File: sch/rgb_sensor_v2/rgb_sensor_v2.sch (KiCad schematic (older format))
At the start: 57 parts, among them J1 Conn_01x20_Male, Q1 2N7002, Q2 2N7002, Q3 2N7002, Q4 2N7002, Q5 2N7002, U1 TCS34725FN, U2 TCS34725FN, U3 TCS34725FN, U4 TCS34725FN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

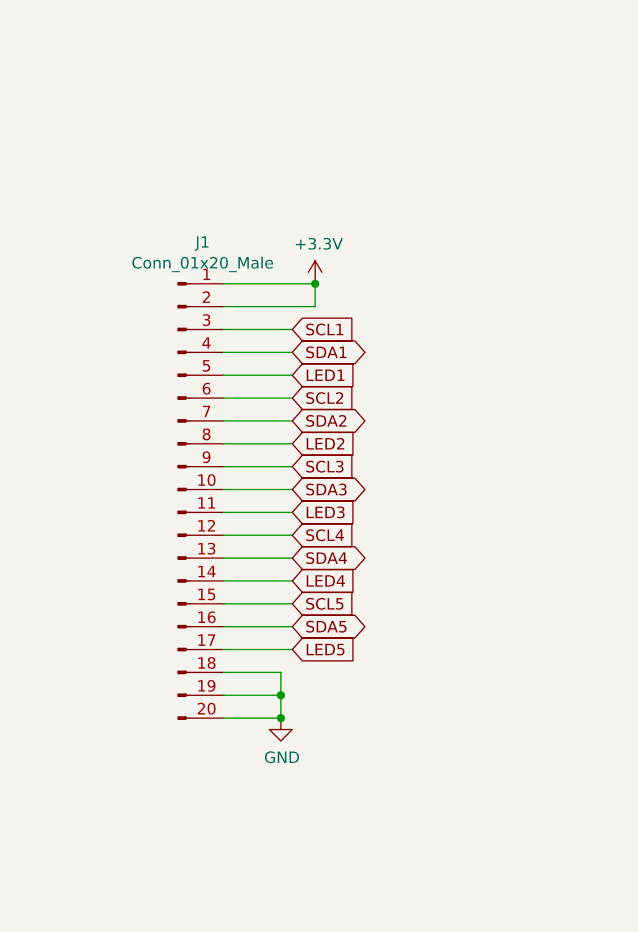
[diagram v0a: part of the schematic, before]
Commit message: some layout done
beefore changing pin assignment on main connector
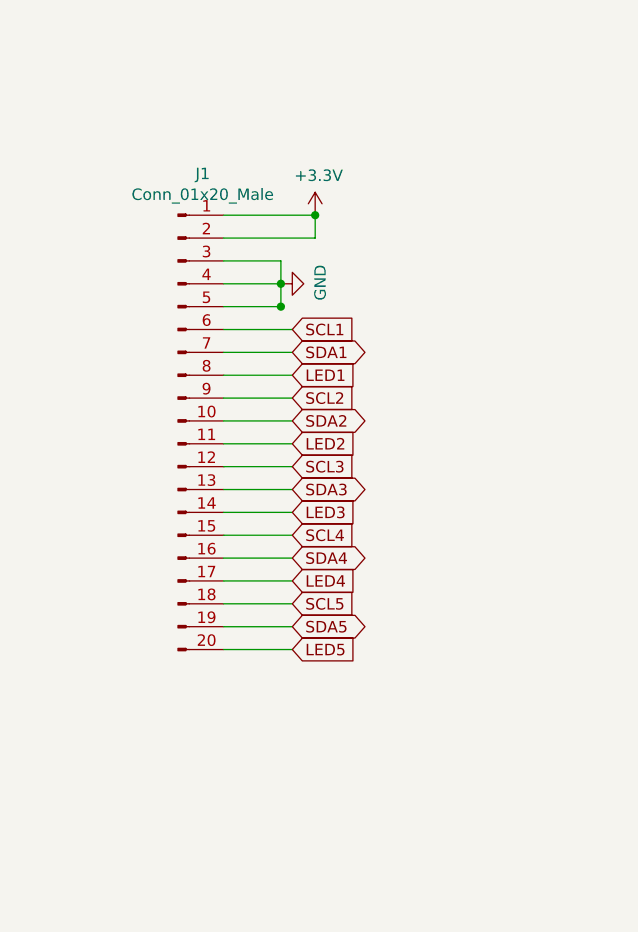
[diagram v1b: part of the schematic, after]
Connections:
- net GND: now also J1.3 (Pin_3), J1.4 (Pin_4), J1.5 (Pin_5); no longer J1.18 (Pin_18), J1.19 (Pin_19), J1.20 (Pin_20)
- net LED1: now also J1.8 (Pin_8); no longer J1.5 (Pin_5)
- net LED2: now also J1.11 (Pin_11); no longer J1.8 (Pin_8)
- net LED3: now also J1.14 (Pin_14); no longer J1.11 (Pin_11)
- net LED4: now also J1.17 (Pin_17); no longer J1.14 (Pin_14)
- net LED5: now also J1.20 (Pin_20); no longer J1.17 (Pin_17)
- net SCL1: now also J1.6 (Pin_6); no longer J1.3 (Pin_3)
- net SCL2: now also J1.9 (Pin_9); no longer J1.6 (Pin_6)
- net SCL3: now also J1.12 (Pin_12); no longer J1.9 (Pin_9)
- net SCL4: now also J1.15 (Pin_15); no longer J1.12 (Pin_12)
- net SCL5: now also J1.18 (Pin_18); no longer J1.15 (Pin_15)
- net SDA1: now also J1.7 (Pin_7); no longer J1.4 (Pin_4)
- net SDA2: now also J1.10 (Pin_10); no longer J1.7 (Pin_7)
- net SDA3: now also J1.13 (Pin_13); no longer J1.10 (Pin_10)
- net SDA4: now also J1.16 (Pin_16); no longer J1.13 (Pin_13)
- net SDA5: now also J1.19 (Pin_19); no longer J1.16 (Pin_16)
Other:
- moved on the sheet: J1
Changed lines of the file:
@@
 L power:+3.3V #PWR021
 U 1 1 5FB4782C
-P 2350 4350
-F 0 "#PWR021" H 2350 4200 50  0001 C CNN
-F 1 "+3.3V" H 2365 4523 50  0000 C CNN
-F 2 "" H 2350 4350 50  0001 C CNN
-F 3 "" H 2350 4350 50  0001 C CNN
-	1    2350 4350
+P 2350 4050
+F 0 "#PWR021" H 2350 3900 50  0001 C CNN
+F 1 "+3.3V" H 2365 4223 50  0000 C CNN
+F 2 "" H 2350 4050 50  0001 C CNN
+F 3 "" H 2350 4050 50  0001 C CNN
+	1    2350 4050
 	1    0    0    -1
 $EndComp
@@
 L power:GND #PWR032
 U 1 1 5FB48129
-P 2200 6250
-F 0 "#PWR032" H 2200 6000 50  0001 C CNN
-F 1 "GND" H 2205 6077 50  0000 C CNN
-F 2 "" H 2200 6250 50  0001 C CNN
-F 3 "" H 2200 6250 50  0001 C CNN
-	1    2200 6250
-	1    0    0    -1
+P 2200 4350
+F 0 "#PWR032" H 2200 4100 50  0001 C CNN
+F 1 "GND" H 2205 4177 50  0000 C CNN
+F 2 "" H 2200 4350 50  0001 C CNN
+F 3 "" H 2200 4350 50  0001 C CNN
+	1    2200 4350
+	0    -1   -1   0
 $EndComp
 Wire Wire Line
@@
 L Connector:Conn_01x20_Male J1
 U 1 1 5FB2920F
-P 1750 5250
-F 0 "J1" H 1858 6331 50  0000 C CNN
-F 1 "Conn_01x20_Male" H 1858 6240 50  0000 C CNN
-F 2 "Connector_PinHeader_2.00mm:PinHeader_2x10_P2.00mm_Horizontal" H 1750 5250 50  0001 C CNN
-F 3 "~" H 1750 5250 50  0001 C CNN
-	1    1750 5250
+P 1750 4950
+F 0 "J1" H 1858 6031 50  0000 C CNN
+F 1 "Conn_01x20_Male" H 1858 5940 50  0000 C CNN
+F 2 "Connector_PinHeader_2.00mm:PinHeader_2x10_P2.00mm_Horizontal" H 1750 4950 50  0001 C CNN
+F 3 "~" H 1750 4950 50  0001 C CNN
+	1    1750 4950
 	1    0    0    -1
 $EndComp
@@
 	1950 5950 2250 5950
 Wire Wire Line
-	2200 6250 2200 6150
+	2200 4450 2200 4350
 Wire Wire Line
-	1950 6050 2200 6050
+	1950 4250 2200 4250
 Wire Wire Line
-	1950 6150 2200 6150
-Connection ~ 2200 6150
+	1950 4350 2200 4350
+Connection ~ 2200 4350
 Wire Wire Line
-	2200 6150 2200 6050
+	2200 4350 2200 4250
 Wire Wire Line
-	1950 6250 2200 6250
-Connection ~ 2200 6250
+	1950 4450 2200 4450
+Connection ~ 2200 4450
 Wire Wire Line
-	2350 4350 1950 4350
+	2350 4050 1950 4050
 Wire Wire Line
-	1950 4450 2350 4450
+	1950 4150 2350 4150
 Wire Wire Line
-	2350 4450 2350 4350
-Connection ~ 2350 4350
+	2350 4150 2350 4050
+Connection ~ 2350 4050
 Text Notes 1050 850  0    50   ~ 0
 Godziny:\n03/11/20 2h setup projektu i schemat\n04/11/20 1h dobranie footprintow

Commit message: Zapisany postęp godzinowy
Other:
- note added: "Godziny:\n03/11/20 2h setup projektu i schemat\n04/11/20 1h dobranie footprintow\n04/11/20 2h5 layout"
- note removed: "Godziny:\n03/11/20 2h setup projektu i schemat\n04/11/20 1h dobranie footprintow"
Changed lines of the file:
@@
 Connection ~ 2350 4050
 Text Notes 1050 850  0    50   ~ 0
-Godziny:\n03/11/20 2h setup projektu i schemat\n04/11/20 1h dobranie footprintow
+Godziny:\n03/11/20 2h setup projektu i schemat\n04/11/20 1h dobranie footprintow\n04/11/20 2h5 layout
 $Comp
 L Graphic:Logo_Open_Hardware_Small #LOGO1

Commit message: add fab outputs but those are not gerber
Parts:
- removed FID1, FID2: Fiducial, Fiducial:Fiducial_1mm_Mask2mm, symbol Mechanical:Fiducial
- removed H3, H4: MountingHole, MountingHole:MountingHole_2.2mm_M2_DIN965_Pad, symbol Mechanical:MountingHole
- J1: footprint Connector_PinHeader_2.00mm:PinHeader_2x10_P2.00mm_Horizontal -> Connector_JST:JST_PHD_S20B-PHDSS_2x10_P2.00mm_Horizontal
- U1, U2, U3, U4, U5: symbol TCS:TCS34725FN -> rgb_sensor_v2-rescue:TCS34725FN-TCS
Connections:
- net GND: now also J1.6 (Pin_6); no longer J1.5 (Pin_5)
- net LED1: now also J1.5 (Pin_5); no longer J1.8 (Pin_8)
- net LED2: now also J1.8 (Pin_8); no longer J1.11 (Pin_11)
- net LED3: now also J1.7 (Pin_7); no longer J1.14 (Pin_14)
- net LED4: now also J1.10 (Pin_10); no longer J1.17 (Pin_17)
- net LED5: now also J1.9 (Pin_9); no longer J1.20 (Pin_20)
- net SCL1: now also J1.20 (Pin_20); no longer J1.6 (Pin_6)
- net SCL2: now also J1.18 (Pin_18); no longer J1.9 (Pin_9)
- net SCL3: now also J1.16 (Pin_16); no longer J1.12 (Pin_12)
- net SCL4: now also J1.14 (Pin_14); no longer J1.15 (Pin_15)
- net SCL5: now also J1.12 (Pin_12); no longer J1.18 (Pin_18)
- net SDA1: now also J1.19 (Pin_19); no longer J1.7 (Pin_7)
- net SDA2: now also J1.17 (Pin_17); no longer J1.10 (Pin_10)
- net SDA3: now also J1.15 (Pin_15); no longer J1.13 (Pin_13)
- net SDA4: now also J1.13 (Pin_13); no longer J1.16 (Pin_16)
- net SDA5: now also J1.11 (Pin_11); no longer J1.19 (Pin_19)
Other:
- note added: "Godziny:\n03/11/20 2h setup projektu i schemat\n04/11/20 1h dobranie footprintow\n04/11/20 2h5 layout \n05/10/20 1h5 koniec routingu"
- note removed: "Godziny:\n03/11/20 2h setup projektu i schemat\n04/11/20 1h dobranie footprintow\n04/11/20 2h5 layout"
- moved on the sheet: H1, H2
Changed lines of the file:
@@
 $EndComp
 $Comp
-L TCS:TCS34725FN U1
+L rgb_sensor_v2-rescue:TCS34725FN-TCS U1
 U 1 1 5FA22706
 P 7150 1150
@@
 $EndComp
 $Comp
-L TCS:TCS34725FN U2
+L rgb_sensor_v2-rescue:TCS34725FN-TCS U2
 U 1 1 5FAF4BF1
 P 7150 3000
@@
 $EndComp
 $Comp
-L TCS:TCS34725FN U3
+L rgb_sensor_v2-rescue:TCS34725FN-TCS U3
 U 1 1 5FAFD847
 P 7150 4950
@@
 $EndComp
 $Comp
-L TCS:TCS34725FN U4
+L rgb_sensor_v2-rescue:TCS34725FN-TCS U4
 U 1 1 5FB06D78
 P 7150 6950
@@
 $EndComp
 $Comp
-L TCS:TCS34725FN U5
+L rgb_sensor_v2-rescue:TCS34725FN-TCS U5
 U 1 1 5FB12878
 P 7150 9000
@@
 Text GLabel 5450 1350 0    50   Input ~ 0
 SCL1
-Text GLabel 2250 4750 2    50   Input ~ 0
-LED1
-Text GLabel 2250 4650 2    50   BiDi ~ 0
+Text GLabel 2250 5850 2    50   BiDi ~ 0
 SDA1
-Text GLabel 2250 4550 2    50   Input ~ 0
-SCL1
+Text GLabel 2250 5250 2    50   BiDi ~ 0
+SDA4
+Text GLabel 2250 4950 2    50   Input ~ 0
+LED4
+Text GLabel 2250 5150 2    50   Input ~ 0
+SCL5
+Text GLabel 2250 5050 2    50   BiDi ~ 0
+SDA5
 Text GLabel 2250 4850 2    50   Input ~ 0
-SCL2
-Text GLabel 2250 4950 2    50   BiDi ~ 0
-SDA2
-Text GLabel 2250 5050 2    50   Input ~ 0
-LED2
-Text GLabel 2250 5150 2    50   Input ~ 0
-SCL3
-Text GLabel 2250 5250 2    50   BiDi ~ 0
-SDA3
-Text GLabel 2250 5350 2    50   Input ~ 0
-LED3
-Text GLabel 2250 5450 2    50   Input ~ 0
-SCL4
-Text GLabel 2250 5550 2    50   BiDi ~ 0
-SDA4
-Text GLabel 2250 5650 2    50   Input ~ 0
-LED4
-Text GLabel 2250 5750 2    50   Input ~ 0
-SCL5
-Text GLabel 2250 5850 2    50   BiDi ~ 0
-SDA5
-Text GLabel 2250 5950 2    50   Input ~ 0
 LED5
 $Comp
@@
 L power:GND #PWR032
 U 1 1 5FB48129
-P 2200 4350
-F 0 "#PWR032" H 2200 4100 50  0001 C CNN
-F 1 "GND" H 2205 4177 50  0000 C CNN
-F 2 "" H 2200 4350 50  0001 C CNN
-F 3 "" H 2200 4350 50  0001 C CNN
-	1    2200 4350
+P 1950 4250
+F 0 "#PWR032" H 1950 4000 50  0001 C CNN
+F 1 "GND" H 1955 4077 50  0000 C CNN
+F 2 "" H 1950 4250 50  0001 C CNN
+F 3 "" H 1950 4250 50  0001 C CNN
+	1    1950 4250
 	0    -1   -1   0
 $EndComp
 Wire Wire Line
-	2250 4550 1950 4550
+	2250 4450 1950 4450
 $Comp
 L Connector:Conn_01x20_Male J1
@@
 F 0 "J1" H 1858 6031 50  0000 C CNN
 F 1 "Conn_01x20_Male" H 1858 5940 50  0000 C CNN
-F 2 "Connector_PinHeader_2.00mm:PinHeader_2x10_P2.00mm_Horizontal" H 1750 4950 50  0001 C CNN
+F 2 "Connector_JST:JST_PHD_S20B-PHDSS_2x10_P2.00mm_Horizontal" H 1750 4950 50  0001 C CNN
 F 3 "~" H 1750 4950 50  0001 C CNN
 	1    1750 4950
@@
 Wire Wire Line
 	1950 5950 2250 5950
-Wire Wire Line
-	2200 4450 2200 4350
-Wire Wire Line
-	1950 4250 2200 4250
-Wire Wire Line
-	1950 4350 2200 4350
-Connection ~ 2200 4350
-Wire Wire Line
-	2200 4350 2200 4250
-Wire Wire Line
-	1950 4450 2200 4450
-Connection ~ 2200 4450
 Wire Wire Line
 	2350 4050 1950 4050
@@
 Connection ~ 2350 4050
 Text Notes 1050 850  0    50   ~ 0
-Godziny:\n03/11/20 2h setup projektu i schemat\n04/11/20 1h dobranie footprintow\n04/11/20 2h5 layout
+Godziny:\n03/11/20 2h setup projektu i schemat\n04/11/20 1h dobranie footprintow\n04/11/20 2h5 layout \n05/10/20 1h5 koniec routingu
 $Comp
 L Graphic:Logo_Open_Hardware_Small #LOGO1
@@
 $EndComp
 $Comp
-L Mechanical:Fiducial FID2
-U 1 1 5FA54DCF
-P 12850 9800
-F 0 "FID2" H 12935 9846 50  0000 L CNN
-F 1 "Fiducial" H 12935 9755 50  0000 L CNN
-F 2 "Fiducial:Fiducial_1mm_Mask2mm" H 12850 9800 50  0001 C CNN
-F 3 "~" H 12850 9800 50  0001 C CNN
-	1    12850 9800
-	1    0    0    -1
-$EndComp
-$Comp
-L Mechanical:Fiducial FID1
-U 1 1 5FA551AA
-P 12850 9600
-F 0 "FID1" H 12935 9646 50  0000 L CNN
-F 1 "Fiducial" H 12935 9555 50  0000 L CNN
-F 2 "Fiducial:Fiducial_1mm_Mask2mm" H 12850 9600 50  0001 C CNN
-F 3 "~" H 12850 9600 50  0001 C CNN
-	1    12850 9600
-	1    0    0    -1
-$EndComp
-$Comp
-L Mechanical:MountingHole H4
-U 1 1 5FA56C7E
+L Mechanical:MountingHole H2
+U 1 1 5FA5842C
 P 12000 9800
-F 0 "H4" H 12100 9846 50  0000 L CNN
+F 0 "H2" H 12100 9846 50  0000 L CNN
 F 1 "MountingHole" H 12100 9755 50  0000 L CNN
 F 2 "MountingHole:MountingHole_2.2mm_M2_DIN965_Pad" H 12000 9800 50  0001 C CNN
@@
 $EndComp
 $Comp
-L Mechanical:MountingHole H3
-U 1 1 5FA57D28
+L Mechanical:MountingHole H1
+U 1 1 5FA585A6
 P 12000 9600
-F 0 "H3" H 12100 9646 50  0000 L CNN
+F 0 "H1" H 12100 9646 50  0000 L CNN
 F 1 "MountingHole" H 12100 9555 50  0000 L CNN
 F 2 "MountingHole:MountingHole_2.2mm_M2_DIN965_Pad" H 12000 9600 50  0001 C CNN
@@
 	1    0    0    -1
 $EndComp
-$Comp
-L Mechanical:MountingHole H2
-U 1 1 5FA5842C
-P 12000 9400
-F 0 "H2" H 12100 9446 50  0000 L CNN
-F 1 "MountingHole" H 12100 9355 50  0000 L CNN
-F 2 "MountingHole:MountingHole_2.2mm_M2_DIN965_Pad" H 12000 9400 50  0001 C CNN
-F 3 "~" H 12000 9400 50  0001 C CNN
-	1    12000 9400
-	1    0    0    -1
-$EndComp
-$Comp
-L Mechanical:MountingHole H1
-U 1 1 5FA585A6
-P 12000 9200
-F 0 "H1" H 12100 9246 50  0000 L CNN
-F 1 "MountingHole" H 12100 9155 50  0000 L CNN
-F 2 "MountingHole:MountingHole_2.2mm_M2_DIN965_Pad" H 12000 9200 50  0001 C CNN
-F 3 "~" H 12000 9200 50  0001 C CNN
-	1    12000 9200
-	1    0    0    -1
-$EndComp
+Text GLabel 2250 5350 2    50   Input ~ 0
+SCL4
+Text GLabel 2250 4650 2    50   Input ~ 0
+LED3
+Text GLabel 2250 5450 2    50   BiDi ~ 0
+SDA3
+Text GLabel 2250 5550 2    50   Input ~ 0
+SCL3
+Text GLabel 2250 4750 2    50   Input ~ 0
+LED2
+Text GLabel 2250 5650 2    50   BiDi ~ 0
+SDA2
+Text GLabel 2250 5750 2    50   Input ~ 0
+SCL2
+Text GLabel 2250 5950 2    50   Input ~ 0
+SCL1
+Text GLabel 2250 4450 2    50   Input ~ 0
+LED1
+$Comp
+L power:GND #PWR0101
+U 1 1 5FB4CB45
+P 1950 4550
+F 0 "#PWR0101" H 1950 4300 50  0001 C CNN
+F 1 "GND" H 1955 4377 50  0000 C CNN
+F 2 "" H 1950 4550 50  0001 C CNN
+F 3 "" H 1950 4550 50  0001 C CNN
+	1    1950 4550
+	0    -1   -1   0
+$EndComp
+Wire Wire Line
+	1950 4250 1950 4350
+Connection ~ 1950 4250
 $EndSCHEMATC

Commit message: dodana plytka ctrl i zrobiony routing w 90%
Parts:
- U1, U2, U3, U4, U5: symbol rgb_sensor_v2-rescue:TCS34725FN-TCS -> rgb_sensor_v2-rescue:TCS34725FN-TCS-rgb_sensor_v2-rescue
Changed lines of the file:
@@
 $EndComp
 $Comp
-L rgb_sensor_v2-rescue:TCS34725FN-TCS U1
+L rgb_sensor_v2-rescue:TCS34725FN-TCS-rgb_sensor_v2-rescue U1
 U 1 1 5FA22706
 P 7150 1150
@@
 $EndComp
 $Comp
-L rgb_sensor_v2-rescue:TCS34725FN-TCS U2
+L rgb_sensor_v2-rescue:TCS34725FN-TCS-rgb_sensor_v2-rescue U2
 U 1 1 5FAF4BF1
 P 7150 3000
@@
 $EndComp
 $Comp
-L rgb_sensor_v2-rescue:TCS34725FN-TCS U3
+L rgb_sensor_v2-rescue:TCS34725FN-TCS-rgb_sensor_v2-rescue U3
 U 1 1 5FAFD847
 P 7150 4950
@@
 $EndComp
 $Comp
-L rgb_sensor_v2-rescue:TCS34725FN-TCS U4
+L rgb_sensor_v2-rescue:TCS34725FN-TCS-rgb_sensor_v2-rescue U4
 U 1 1 5FB06D78
 P 7150 6950
@@
 $EndComp
 $Comp
-L rgb_sensor_v2-rescue:TCS34725FN-TCS U5
+L rgb_sensor_v2-rescue:TCS34725FN-TCS-rgb_sensor_v2-rescue U5
 U 1 1 5FB12878
 P 7150 9000
@@
 	2350 4150 2350 4050
 Connection ~ 2350 4050
-Text Notes 1050 850  0    50   ~ 0
+Text Notes 550  950  0    50   ~ 0
 Godziny:\n03/11/20 2h setup projektu i schemat\n04/11/20 1h dobranie footprintow\n04/11/20 2h5 layout \n05/10/20 1h5 koniec routingu
 $Comp

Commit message: bom
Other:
- note added: "DS1014-20RF1B CONNFLY"
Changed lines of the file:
@@
 	1950 4250 1950 4350
 Connection ~ 1950 4250
+Text Notes 2600 5100 0    50   ~ 0
+DS1014-20RF1B CONNFLY
 $EndSCHEMATC
